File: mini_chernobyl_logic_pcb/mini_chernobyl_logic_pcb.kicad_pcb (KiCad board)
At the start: 2 copper layers, 148 x 49 mm, 21 parts, among them U1 MAX7219, U2 74AHCT125, U3 74AHCT125, U4 ADAFRUIT-FEATHER-328

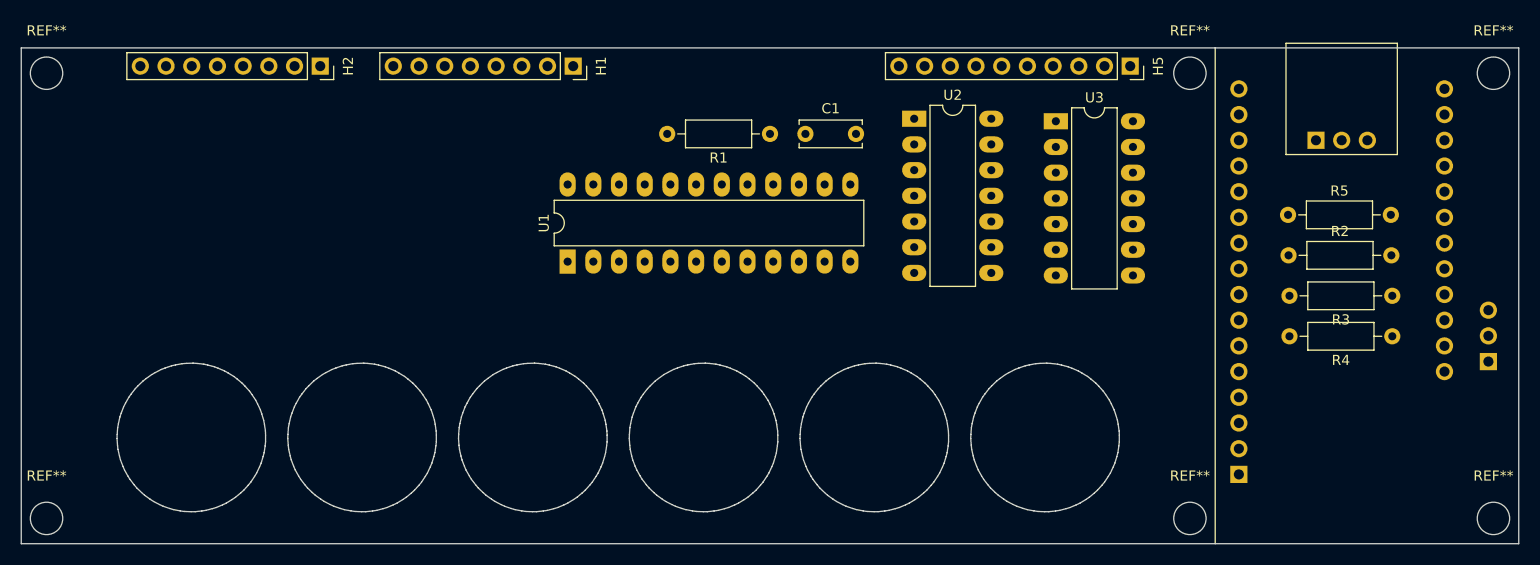
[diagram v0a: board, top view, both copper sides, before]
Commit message: route logic board
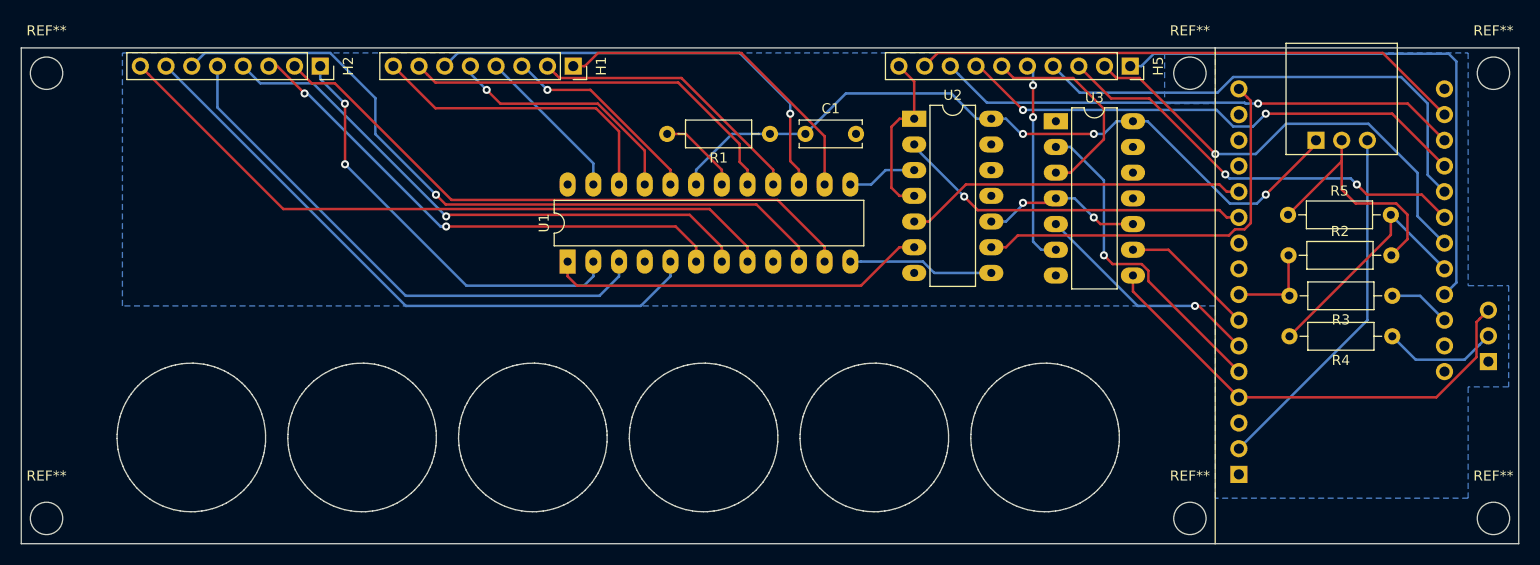
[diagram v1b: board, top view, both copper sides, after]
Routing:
- net +5V: track 0.00 -> 74.2 mm, vias 0 -> 3
- net Net-(H2-Pad6): track 0.00 -> 72.0 mm, vias 0 -> 1
- net Net-(H2-Pad8): track 0.00 -> 68.9 mm
- net Net-(H2-Pad7): track 0.00 -> 62.8 mm
- net Net-(H2-Pad2): track 0.00 -> 61.2 mm
- net GND: track 0.00 -> 57.7 mm, vias 0 -> 2
- net Net-(H5-Pad1): track 0.00 -> 56.6 mm
- net Net-(H2-Pad4): track 0.00 -> 56.3 mm, vias 0 -> 1
- net Net-(H5-Pad9): track 0.00 -> 54.4 mm
- net Net-(H2-Pad5): track 0.00 -> 53.7 mm
- net Net-(H5-Pad8): track 0.00 -> 51.9 mm, vias 0 -> 1
- net Net-(H5-Pad7): track 0.00 -> 51.4 mm, vias 0 -> 2
- net Net-(H2-Pad3): track 0.00 -> 51.1 mm, vias 0 -> 2
- net Net-(H5-Pad4): track 0.00 -> 49.2 mm
- net Net-(H4-Pad3): track 0.00 -> 46.6 mm
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- added copper zone on B.Cu, net GND

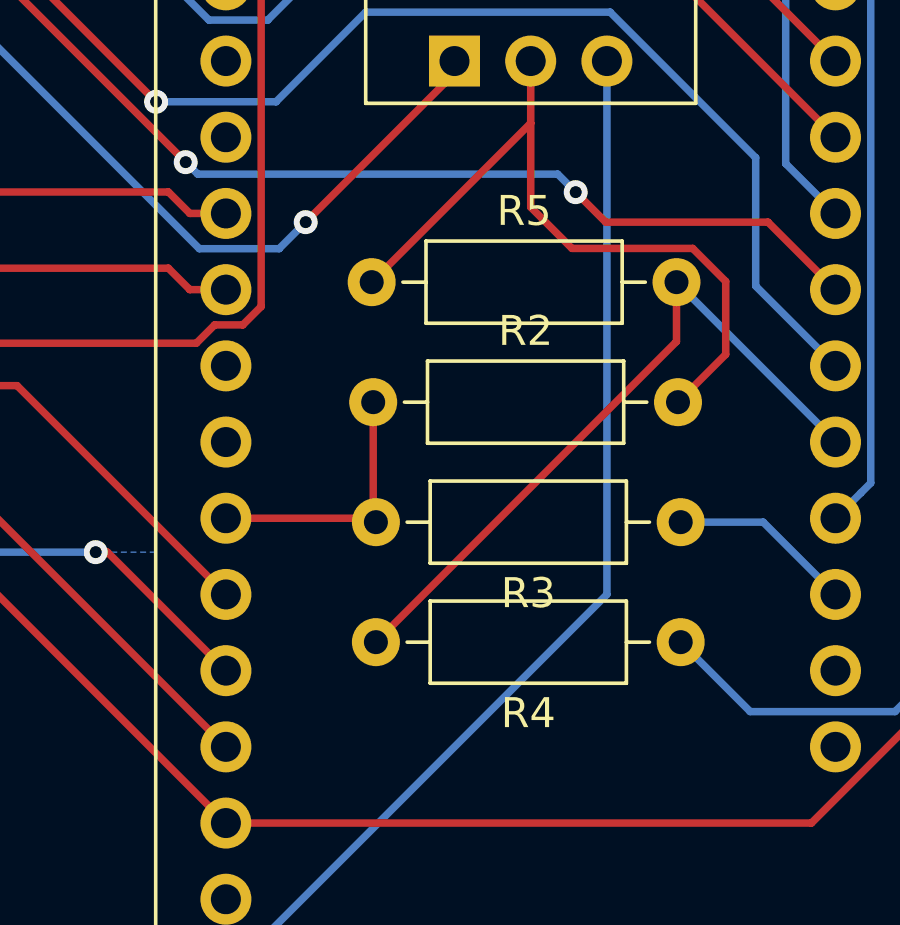
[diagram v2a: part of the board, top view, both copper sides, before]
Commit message: add and clean up labels on pcbs
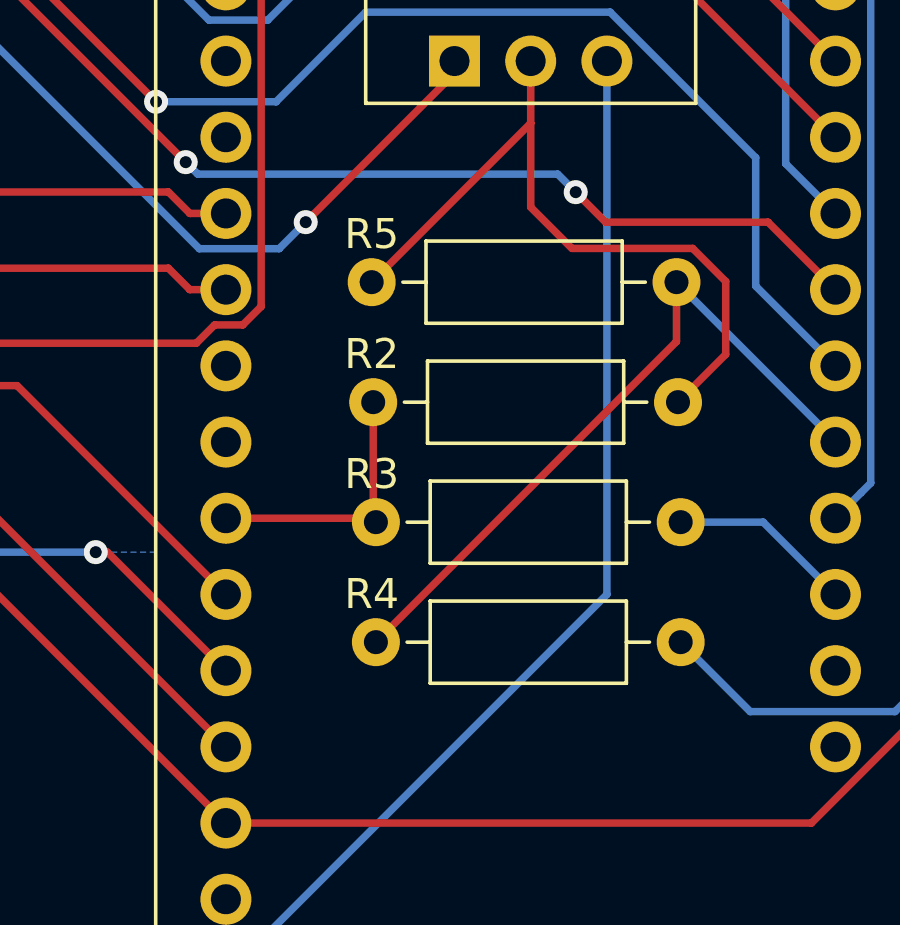
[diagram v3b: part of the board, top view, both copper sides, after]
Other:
- board text added: "3V3"
- board text added: "5V"
- board text added: "GND"
- board text added: "TRG"
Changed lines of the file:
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@@
   (general
     (thickness 1.6)
-    (drawings 527)
+    (drawings 537)
     (tracks 301)
     (zones 0)
@@
     (47 F.CrtYd user)
     (48 B.Fab user)
-    (49 F.Fab user)
+    (49 F.Fab user hide)
   )
   (setup
@@
     (descr "Resistor, Axial_DIN0207 series, Axial, Horizontal, pin pitch=10.16mm, 0.25W = 1/4W, length*diameter=6.3*2.5mm^2, http://cdn-reichelt.de/documents/datenblatt/B400/1_4W%23YAG.pdf")
     (tags "Resistor Axial_DIN0207 series Axial Horizontal pin pitch 10.16mm 0.25W = 1/4W length 6.3mm diameter 2.5mm")
-    (fp_text reference R2 (at 5.08 -2.37) (layer F.SilkS)
+    (fp_text reference R2 (at -0.05 -1.6) (layer F.SilkS)
       (effects (font (size 1 1) (thickness 0.15)))
     )
@@
     (descr "Resistor, Axial_DIN0207 series, Axial, Horizontal, pin pitch=10.16mm, 0.25W = 1/4W, length*diameter=6.3*2.5mm^2, http://cdn-reichelt.de/documents/datenblatt/B400/1_4W%23YAG.pdf")
     (tags "Resistor Axial_DIN0207 series Axial Horizontal pin pitch 10.16mm 0.25W = 1/4W length 6.3mm diameter 2.5mm")
-    (fp_text reference R3 (at 5.08 -2.37) (layer F.SilkS)
+    (fp_text reference R3 (at 10.3 1.6) (layer F.SilkS)
       (effects (font (size 1 1) (thickness 0.15)))
     )
@@
     (descr "Resistor, Axial_DIN0207 series, Axial, Horizontal, pin pitch=10.16mm, 0.25W = 1/4W, length*diameter=6.3*2.5mm^2, http://cdn-reichelt.de/documents/datenblatt/B400/1_4W%23YAG.pdf")
     (tags "Resistor Axial_DIN0207 series Axial Horizontal pin pitch 10.16mm 0.25W = 1/4W length 6.3mm diameter 2.5mm")
-    (fp_text reference R4 (at 5.08 -2.37) (layer F.SilkS)
+    (fp_text reference R4 (at 10.3 1.6) (layer F.SilkS)
       (effects (font (size 1 1) (thickness 0.15)))
     )
@@
     (descr "Resistor, Axial_DIN0207 series, Axial, Horizontal, pin pitch=10.16mm, 0.25W = 1/4W, length*diameter=6.3*2.5mm^2, http://cdn-reichelt.de/documents/datenblatt/B400/1_4W%23YAG.pdf")
     (tags "Resistor Axial_DIN0207 series Axial Horizontal pin pitch 10.16mm 0.25W = 1/4W length 6.3mm diameter 2.5mm")
-    (fp_text reference R5 (at 5.08 -2.37) (layer F.SilkS)
+    (fp_text reference R5 (at 0 -1.6) (layer F.SilkS)
       (effects (font (size 1 1) (thickness 0.15)))
     )
@@
     )
   )
+  (gr_text 5V (at 238.75 109.25) (layer B.SilkS)
+    (effects (font (size 1 1) (thickness 0.15)) (justify mirror))
+  )
+  (gr_text TRG (at 238.25 112) (layer B.SilkS)
+    (effects (font (size 1 1) (thickness 0.15)) (justify mirror))
+  )
+  (gr_text GND (at 238.25 114.5) (layer B.SilkS)
+    (effects (font (size 1 1) (thickness 0.15)) (justify mirror))
+  )
+  (gr_line (start 232 83.05) (end 221 83.05) (layer B.SilkS) (width 0.12))
+  (gr_line (start 232 94.05) (end 232 83.05) (layer B.SilkS) (width 0.12))
+  (gr_line (start 221 94.05) (end 232 94.05) (layer B.SilkS) (width 0.12))
+  (gr_line (start 221 83.05) (end 221 94.05) (layer B.SilkS) (width 0.12))
+  (gr_text 3V3 (at 229 89.5 90) (layer B.SilkS)
+    (effects (font (size 1 1) (thickness 0.15)) (justify mirror))
+  )
+  (gr_text GND (at 226.5 89.5 90) (layer B.SilkS)
+    (effects (font (size 1 1) (thickness 0.15)) (justify mirror))
+  )
+  (gr_text 5V (at 224 90 90) (layer B.SilkS)
+    (effects (font (size 1 1) (thickness 0.15)) (justify mirror))
+  )
   (gr_line (start 221 83.04) (end 221 94.04) (layer F.SilkS) (width 0.12))

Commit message: sync project; add firmware
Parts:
- H1, H2: footprint Connector_PinSocket_2.54mm:PinSocket_1x08_P2.54mm_Vertical -> mini_chernobyl_logic_pcb:8-PIN-CONNECTOR
- H5: footprint Connector_PinSocket_2.54mm:PinSocket_1x10_P2.54mm_Vertical -> mini_chernobyl_logic_pcb:10-PIN-CONNECTOR
- moved H3 7.17 mm to (229.0, 87.6), turned to 90 degrees
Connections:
- U4 pad 4: Net-(H4-Pad3) -> GND
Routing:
- net GND: track 57.7 -> 82.8 mm, vias 2 -> 3
- net +5V: track 74.2 -> 83.4 mm, vias 3 -> 4
- net Net-(H3-Pad3): track 35.7 -> 42.9 mm
- net Net-(H4-Pad3): track 46.6 -> 43.1 mm
- net Net-(H5-Pad9): track 54.4 -> 56.9 mm
- net Net-(H1-Pad2): track 28.0 -> 28.9 mm, vias 0 -> 1
- net Net-(H5-Pad5): track 20.2 -> 21.0 mm, vias 2 -> 1
- net Net-(H5-Pad6): track 21.0 -> 20.5 mm, vias 0 -> 1
- net Net-(H5-Pad2): vias 1 -> 3
